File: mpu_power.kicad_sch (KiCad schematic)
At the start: 50 parts, among them U401 STM32MP135FAE7

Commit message: Update capacitor BOM
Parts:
- C601, C602, C603, C604, C605, C607, C608, C609, C610, C611, C612, C613, C614, C615, C616, C617, C618, C619, C620, C621, C622, C623, C624, C625, C626, C627, C629, C630, C631, C632, C633, C634, C635, C636, C637, C638, C639, C640, C641, C642, C643, C645, C647, C648: footprint (none) -> Capacitor_SMD:C_0603_1608Metric; Digi-Key Part Number (none) -> 490-12330-1-ND; MPN (none) -> GRT188R61H105KE13D; Manufacturer (none) -> Murata Electronics
- C606, C628, C649: footprint (none) -> perfect_footprints:C_0402_1005Metric; Digi-Key Part Number (none) -> 490-10700-1-ND; MPN (none) -> GRM155R71H104KE14D; Manufacturer (none) -> Murata Electronics
- C644, C646: footprint (none) -> Capacitor_SMD:C_0603_1608Metric; Digi-Key Part Number (none) -> 490-7205-1-ND; MPN (none) -> GRM188R6YA475KE15D; Manufacturer (none) -> Murata Electronics

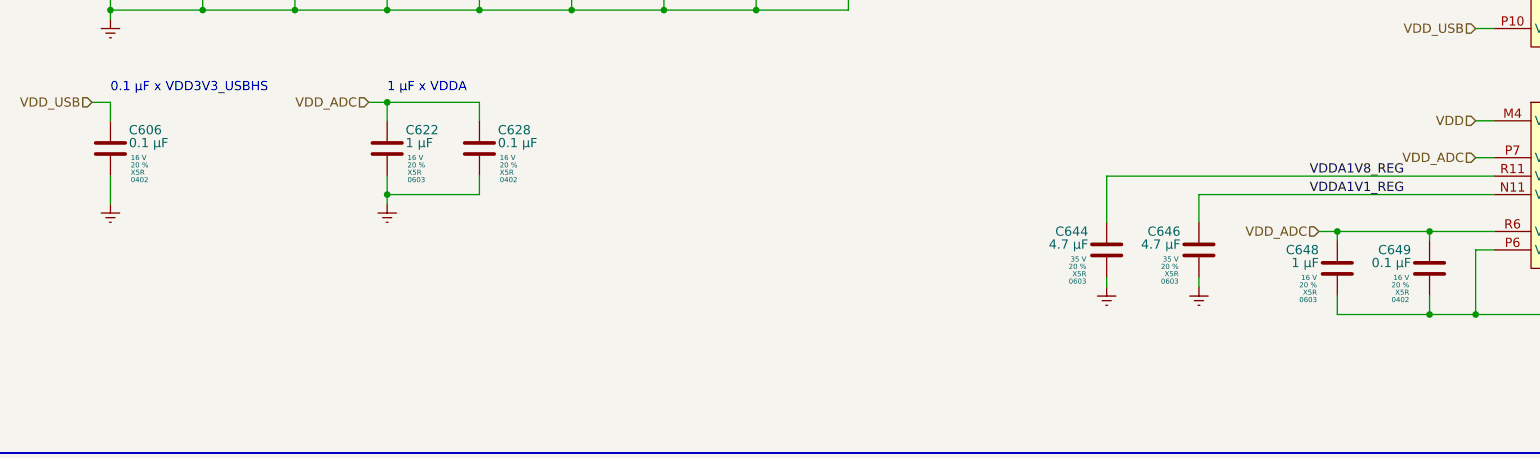
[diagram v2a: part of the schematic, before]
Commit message: 0402 -> 0201 where possible
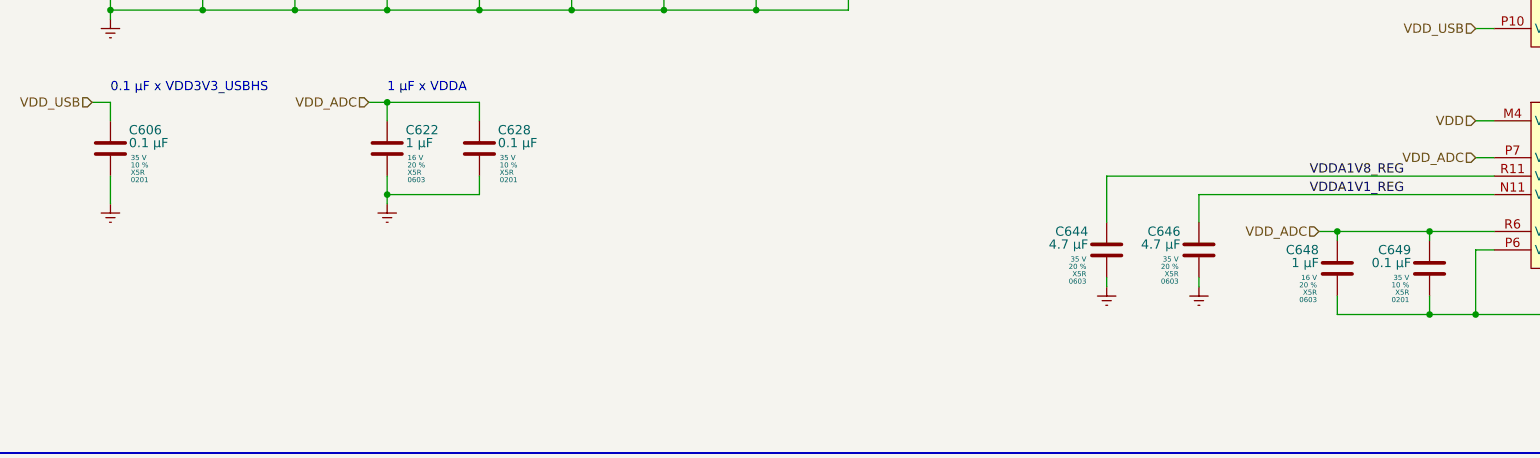
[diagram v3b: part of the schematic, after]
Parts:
- C606, C628, C649: footprint perfect_footprints:C_0402_1005Metric -> Capacitor_SMD:C_0201_0603Metric; Digi-Key Part Number 490-10700-1-ND -> 490-10430-1-ND; MPN GRM155R71H104KE14D -> GRM033R6YA104KE14D; Size 0402 -> 0201; Tolerance 20 % -> 10 %; Voltage rating 16 V -> 35 V

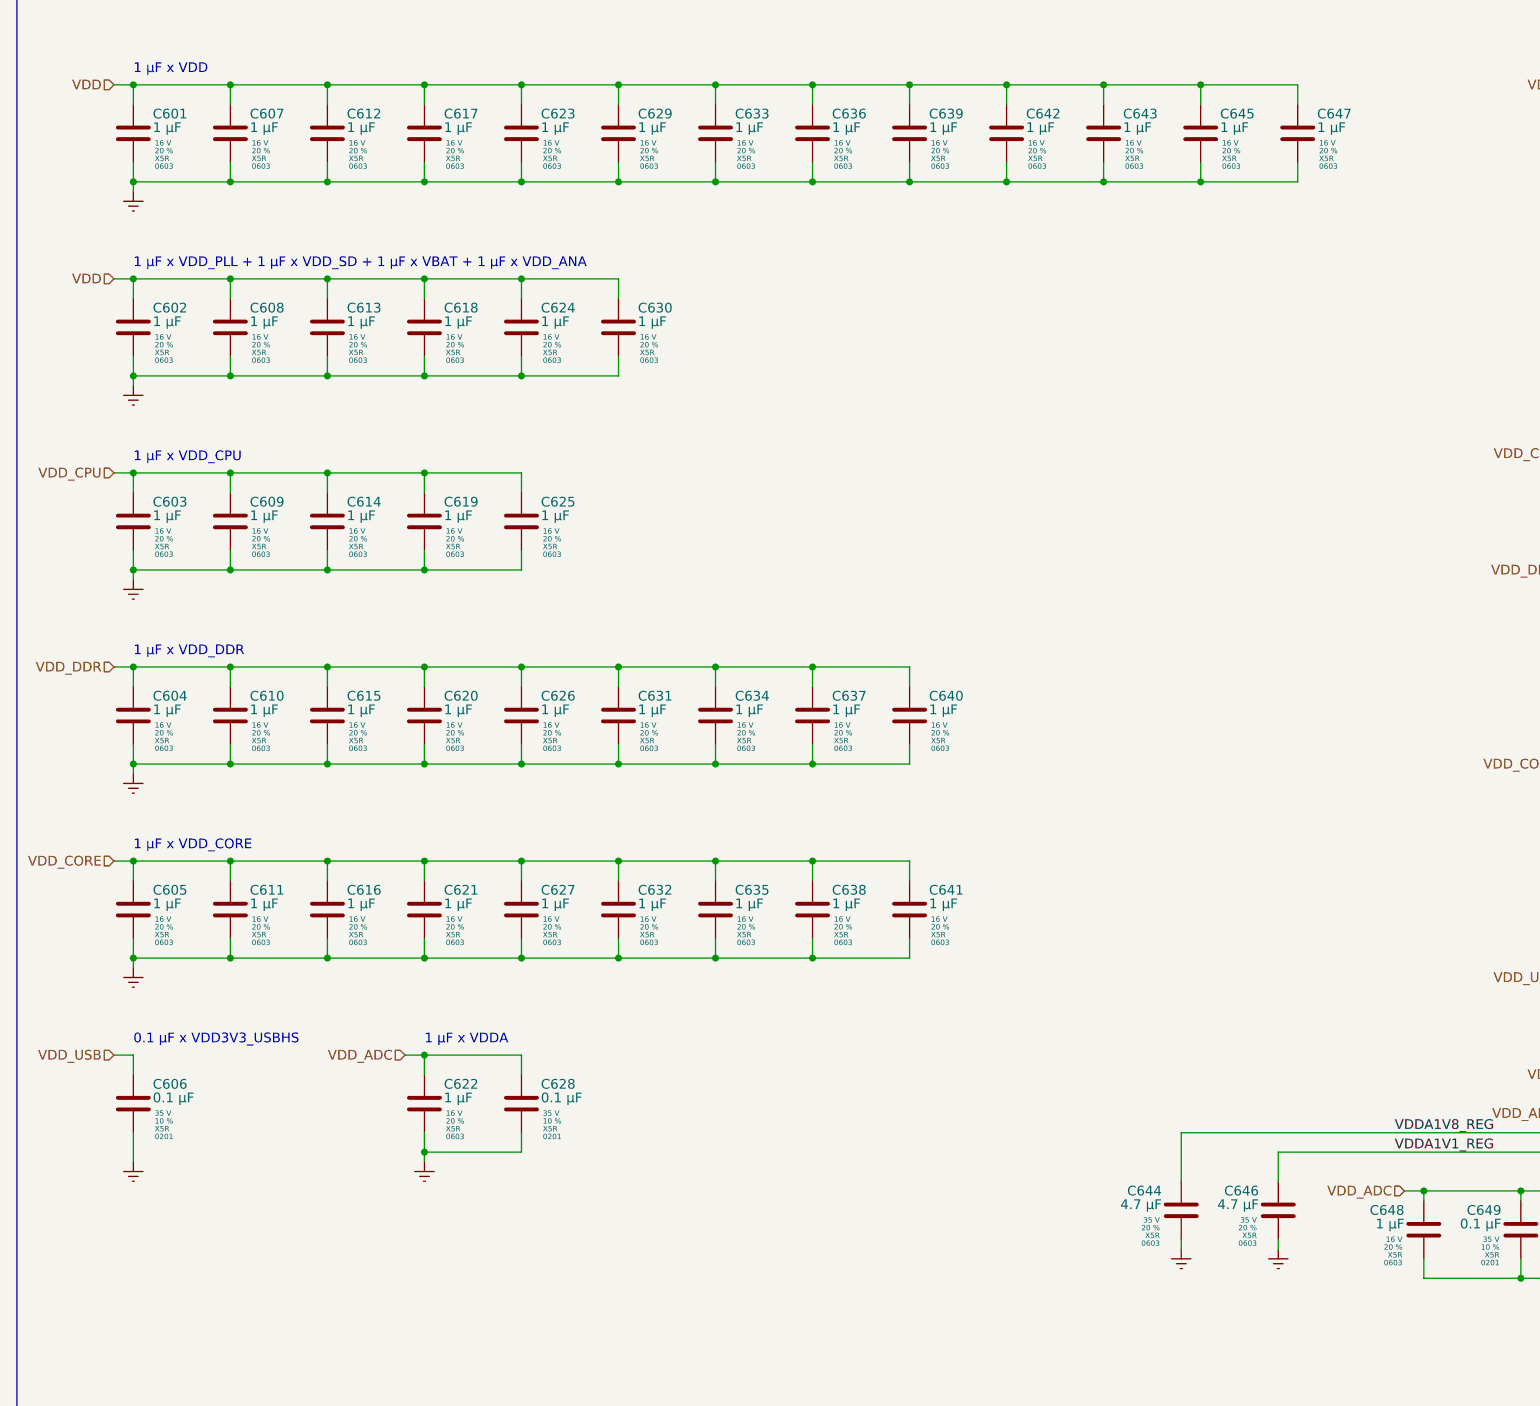
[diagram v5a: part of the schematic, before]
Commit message: Update BOM, and fix MPU pinout
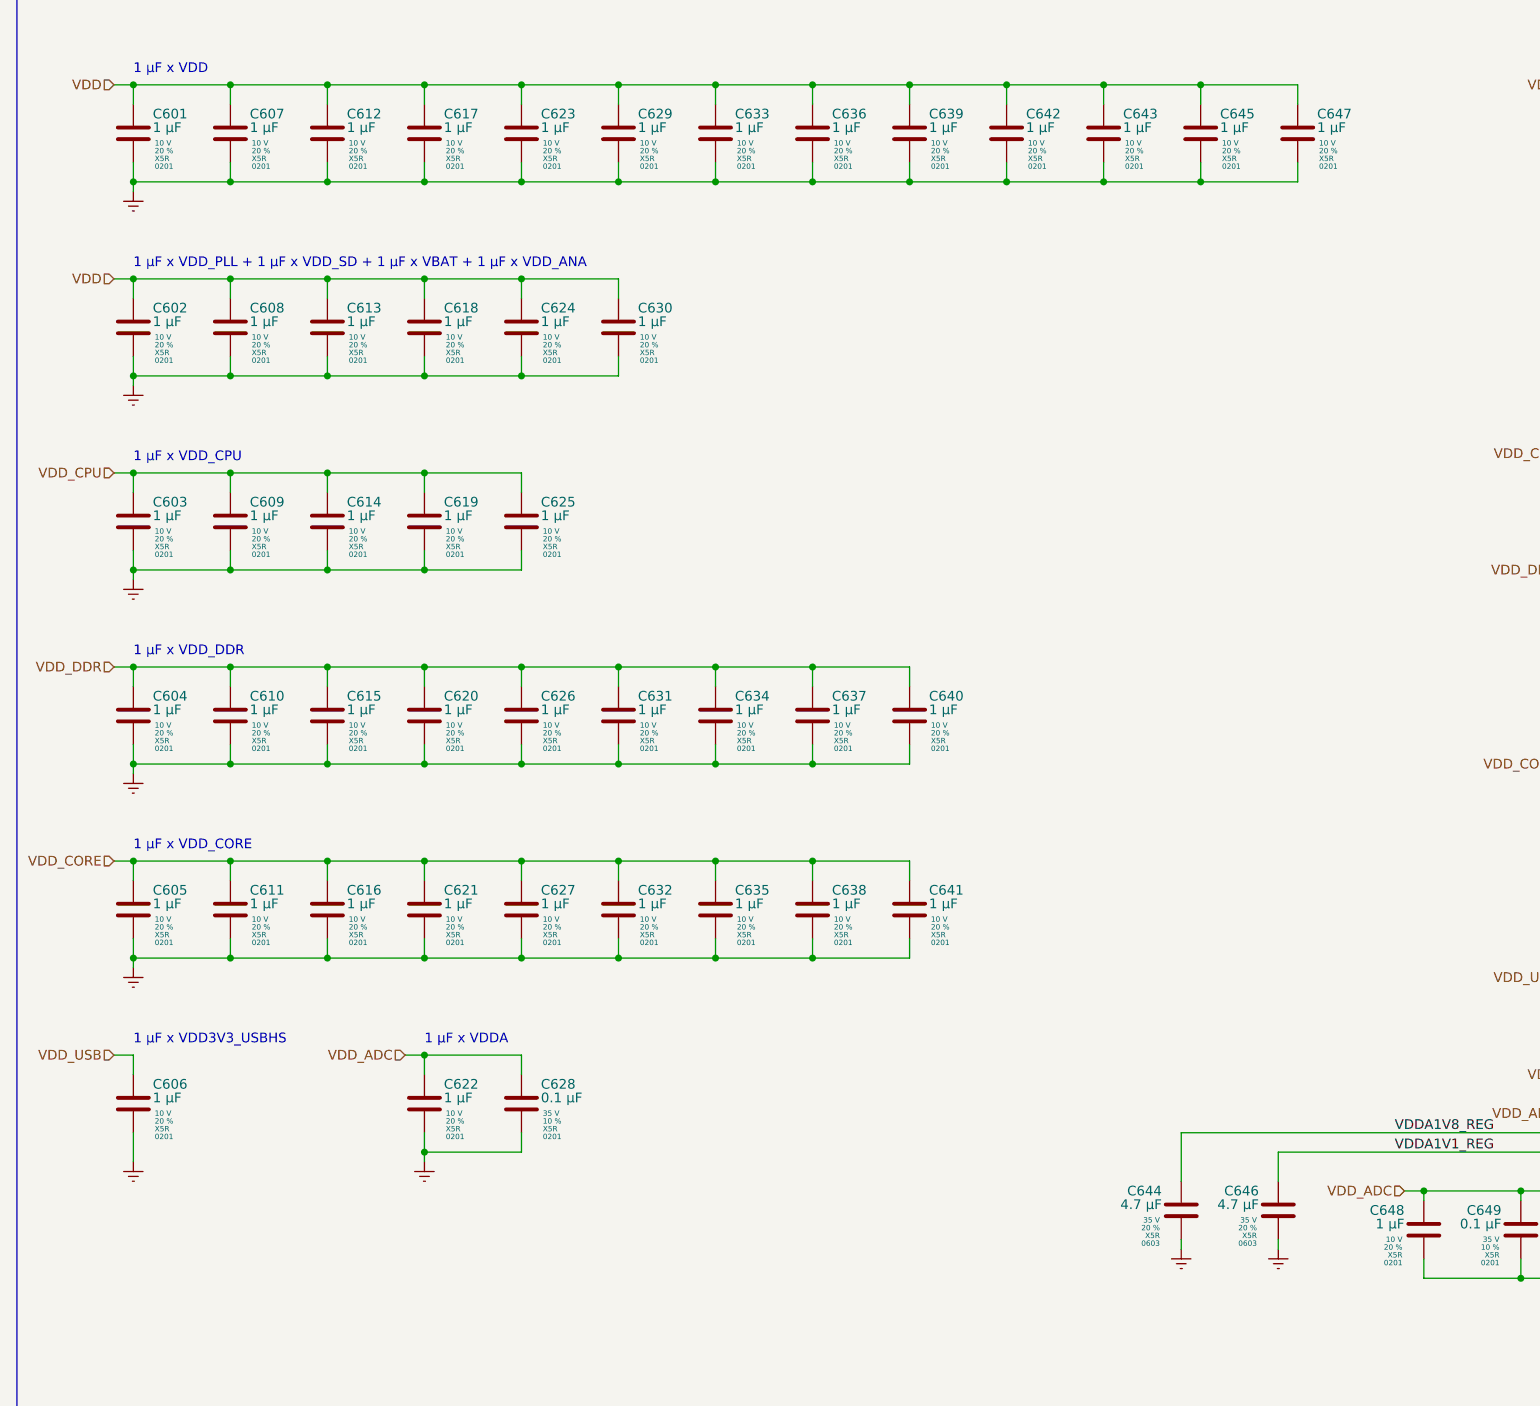
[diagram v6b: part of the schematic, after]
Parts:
- C601, C602, C603, C604, C605, C607, C608, C609, C610, C611, C612, C613, C614, C615, C616, C617, C618, C619, C620, C621, C622, C623, C624, C625, C626, C627, C629, C630, C631, C632, C633, C634, C635, C636, C637, C638, C639, C640, C641, C642, C643, C645, C647, C648: footprint Capacitor_SMD:C_0603_1608Metric -> perfect_footprints:C_0201_0603Metric; Digi-Key Part Number 490-12330-1-ND -> 1276-1324-1-ND; MPN GRT188R61H105KE13D -> CL03A105MP3NSNC; Manufacturer Murata Electronics -> Samsung Electro-Mechanics; Size 0603 -> 0201; Voltage rating 16 V -> 10 V
- C606: value 0.1 µF -> 1 µF; footprint Capacitor_SMD:C_0201_0603Metric -> perfect_footprints:C_0201_0603Metric; Digi-Key Part Number 490-10430-1-ND -> 1276-1324-1-ND; MPN GRM033R6YA104KE14D -> CL03A105MP3NSNC; Manufacturer Murata Electronics -> Samsung Electro-Mechanics; Tolerance 10 % -> 20 %; Voltage rating 35 V -> 10 V
- C628, C649: footprint Capacitor_SMD:C_0201_0603Metric -> perfect_footprints:C_0201_0603Metric
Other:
- note added: "1 µF x VDD3V3_USBHS"
- note removed: "0.1 µF x VDD3V3_USBHS"

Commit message: Rework MPU power
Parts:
- renumbered C631 to C630, C632 to C631, C633 to C632, C634 to C633, C635 to C634, C636 to C635, C637 to C636, C638 to C637, C639 to C638, C640 to C639, C641 to C640, C642 to C641, C643 to C642, C644 to C643, C645 to C644, C646 to C645, C647 to C646, C630 to C647
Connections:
- net VDD: no longer C647.1, U401.C12 (VDDSD1)
- new net VDD_SD_IO: C647.1, U401.C12 (VDDSD1)
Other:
- note added: "1 µF x VDD_PLL + 1 µF x VDD_SD2 + 1 µF x VBAT + 1 µF x VDD_ANA"
- note removed: "1 µF x VDD_PLL + 1 µF x VDD_SD + 1 µF x VBAT + 1 µF x VDD_ANA"
- moved on the sheet: C647
